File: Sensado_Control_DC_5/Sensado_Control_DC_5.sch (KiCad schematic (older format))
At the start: 108 parts, among them J1 Jumper, J2 Jumper, J3 Jumper, P1 R_FUENTE_CON, P10 GPIO, P11 TOR_4, P12 TOR_2, P13 TOR_1, P14 TOR_3, P2 I_+, P3 I_-, P4 POWER, P5 RS-232, P6 I2C, P7 SPI, P8 GND_REG, P9 RESET, Q1 NMOS, Q10 PMOS, Q11 NMOS, Q12 NMOS, Q13 NMOS, Q14 PMOS, Q15 PMOS, Q16 PMOS, Q2 NMOS, Q3 NMOS, Q4 NMOS, Q5 NMOS, Q6 PMOS, Q7 PMOS, Q8 PMOS, Q9 PMOS, U1 Atmega328PA, U2 ACS_712, U3 LD1117S50TR_FINAL, Y1 XRCHA_16M

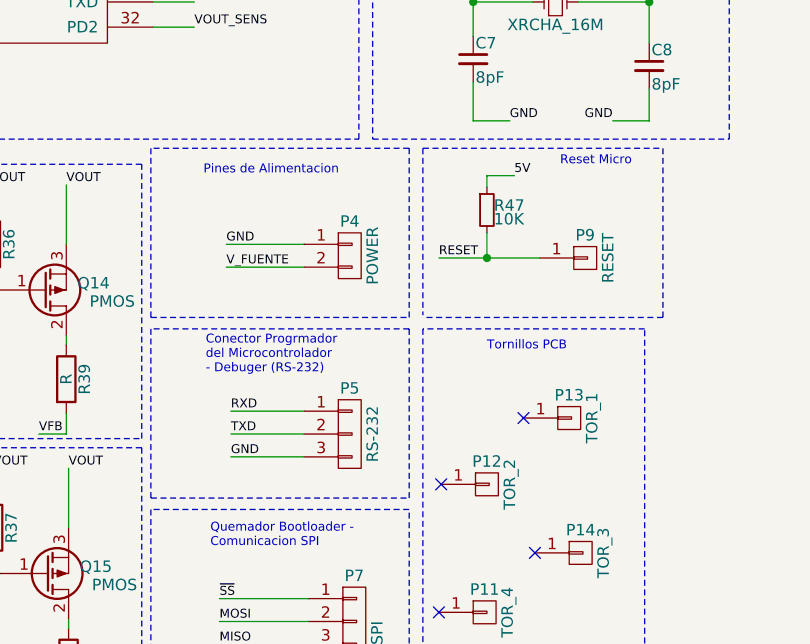
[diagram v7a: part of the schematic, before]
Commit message: Capacitor DTR, Jumper Reset
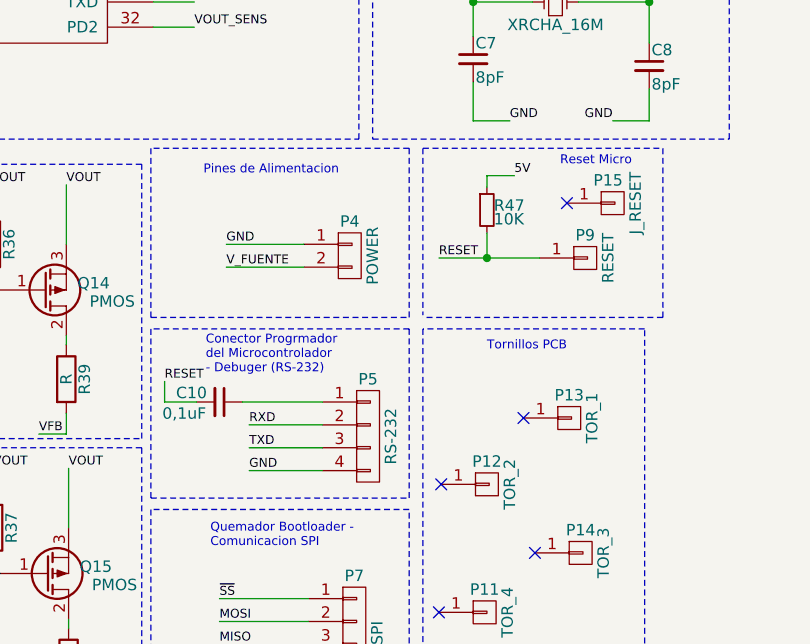
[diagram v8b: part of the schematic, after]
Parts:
- removed P5: RS-232, Socket_Strips:Socket_Strip_Straight_1x03_Pitch2.54mm, symbol CONN_01X03
- added C10: 0,1uF, Capacitors_SMD:C_0805_HandSoldering, symbol 0,1uF
- added P15: J_RESET, Socket_Strips:Socket_Strip_Straight_1x01_Pitch2.54mm, symbol CONN_01X01
- added P5: RS-232, Socket_Strips:Socket_Strip_Straight_1x04_Pitch2.54mm, symbol CONN_01X04
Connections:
- net GND: now also P5.4 (P4)
- net RESET: now also C10.2
- net RXD: now also P5.2 (P2)
- net TXD: now also P5.3 (P3)
- new net: C10.1, P5.1 (P1)
- no-connect marks 6 -> 7
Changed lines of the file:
@@
 Text Label 4660 4400 0    39   ~ 0
 GND
-Text Label 4680 5330 0    39   ~ 0
+Text Label 4760 5390 0    39   ~ 0
 GND
 Text Notes 4560 4100 0    39   ~ 0
@@
 Text Notes 4570 4970 0    39   ~ 0
 Conector Progrmador \ndel Microcontrolador \n- Debuger (RS-232)
-$Comp
-L CONN_01X03 P5
-U 1 1 59D9D14F
-P 5200 5230
-F 0 "P5" H 5200 5430 50  0000 C CNN
-F 1 "RS-232" V 5300 5230 50  0000 C CNN
-F 2 "Socket_Strips:Socket_Strip_Straight_1x03_Pitch2.54mm" H 5200 5230 50  0001 C CNN
-F 3 "" H 5200 5230 50  0000 C CNN
-	1    5200 5230
-	1    0    0    -1
-$EndComp
-Text Label 4680 5230 0    39   ~ 0
+Text Label 4760 5290 0    39   ~ 0
 TXD
-Text Label 4680 5130 0    39   ~ 0
+Text Label 4760 5190 0    39   ~ 0
 RXD
 Text Notes 4590 5730 0    39   ~ 0
@@
 	5460 5510 5460 4770
 Wire Wire Line
-	5000 5330 4680 5330
-Wire Wire Line
-	4680 5230 5000 5230
-Wire Wire Line
-	5000 5130 4680 5130
+	5080 5390 4760 5390
+Wire Wire Line
+	4760 5290 5080 5290
+Wire Wire Line
+	5080 5190 4760 5190
 Wire Notes Line
 	5460 5560 4330 5560
@@
 Text Notes 7690 1350 0    39   ~ 0
 Test Points
+$Comp
+L CONN_01X04 P5
+U 1 1 59D9CDF4
+P 5280 5240
+F 0 "P5" H 5280 5490 50  0000 C CNN
+F 1 "RS-232" V 5380 5240 50  0000 C CNN
+F 2 "Socket_Strips:Socket_Strip_Straight_1x04_Pitch2.54mm" H 5280 5240 50  0001 C CNN
+F 3 "" H 5280 5240 50  0000 C CNN
+	1    5280 5240
+	1    0    0    -1
+$EndComp
+Wire Wire Line
+	4730 5090 5080 5090
+Wire Wire Line
+	4530 5090 4390 5090
+Wire Wire Line
+	4390 5090 4390 5000
+Text Label 4390 5000 0    39   ~ 0
+RESET
+$Comp
+L 0,1uF C10
+U 1 1 59D9EA18
+P 4630 5090
+F 0 "C10" V 4590 4900 50  0000 L CNN
+F 1 "0,1uF" V 4680 4840 50  0000 L CNN
+F 2 "Capacitors_SMD:C_0805_HandSoldering" H 4540 5060 50  0001 C CNN
+F 3 "" H 4630 5090 50  0000 C CNN
+F 4 "478-1395-2-ND" H 4740 5260 118 0001 C CNN "CAP CER 0.1UF 50V X7R 0805"
+	1    4630 5090
+	0    1    1    0
+$EndComp
+$Comp
+L CONN_01X01 P15
+U 1 1 59DA56FE
+P 6350 4220
+F 0 "P15" H 6330 4320 50  0000 C CNN
+F 1 "J_RESET" V 6450 4220 50  0000 C CNN
+F 2 "Socket_Strips:Socket_Strip_Straight_1x01_Pitch2.54mm" H 6350 4220 50  0001 C CNN
+F 3 "" H 6350 4220 50  0000 C CNN
+	1    6350 4220
+	1    0    0    -1
+$EndComp
+NoConn ~ 6150 4220
 $EndSCHEMATC
